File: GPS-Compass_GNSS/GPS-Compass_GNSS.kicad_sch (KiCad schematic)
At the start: 35 parts, among them J1 SMA_F, J3 01x10, Q1 MMBT3904, SW1 GNSS_RST, U1 BGA725L6E6327FTSA1, U2 TESEO-LIV3R

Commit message: asdas
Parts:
- J1: Antenna (none) -> https://cz.mouser.com/ProductDetail/Quectel/YEGT001AA?qs=7D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

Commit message: updates on different boards
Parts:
- added J4: 636101112001, gps-compass_brd:636101112001, symbol gps-compass_sch:636101112001
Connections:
- net GND: now also J4.1, J4.2
- net GNSS_ANT: now also J4.3
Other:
- moved on the sheet: C1, C2, C3, FL1, J1, L1, U1

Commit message: 3d and PCB
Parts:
- removed J1: SMA_F, Connector_Coaxial:SMA_BAT_Wireless_BWSMA-KWE-Z001, symbol Connector:Conn_Coaxial_Small

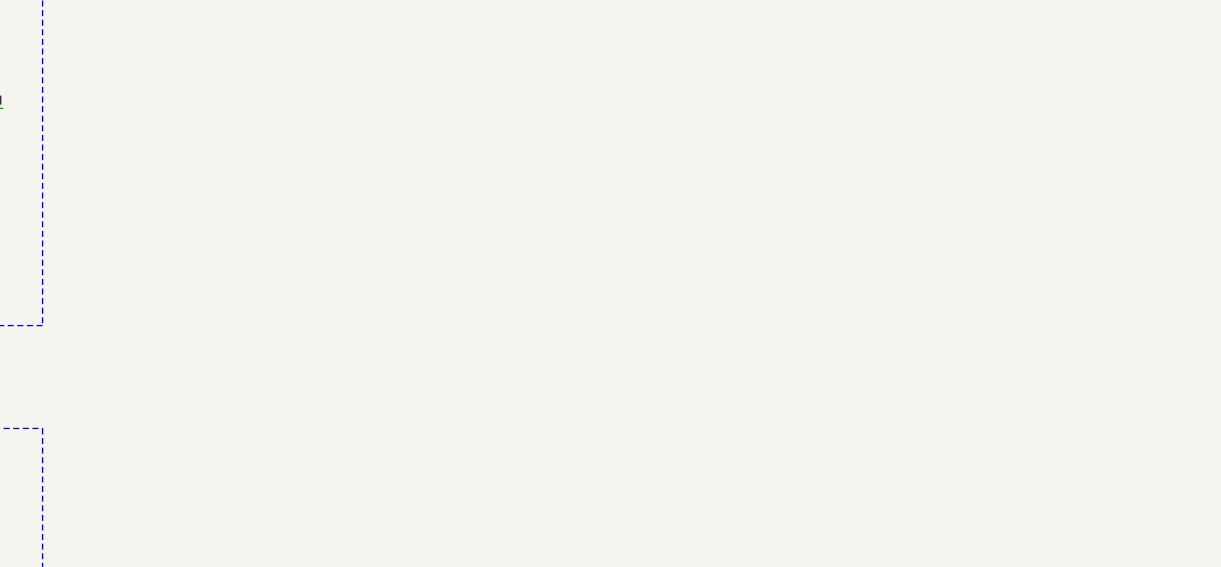
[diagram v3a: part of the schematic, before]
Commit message: new renders and 3d updat4ws
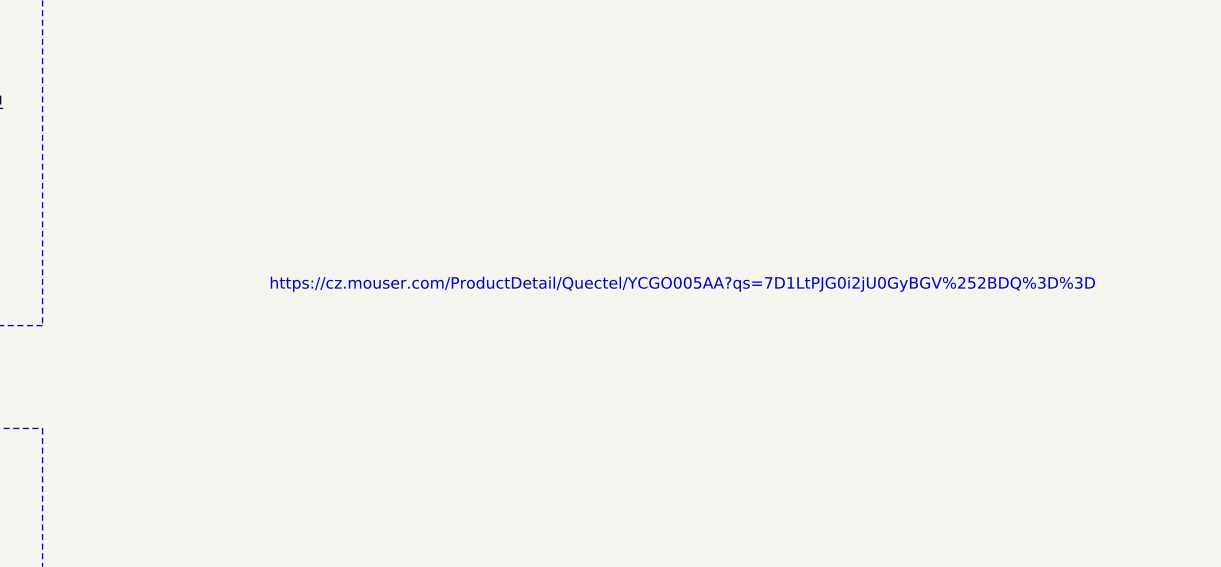
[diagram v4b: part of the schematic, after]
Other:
- note added: "https://cz.mouser.com/ProductDetail/Quectel/YCGO005AA?qs=7D1LtPJG0i2jU0GyBGV%252BDQ%3D%3D"

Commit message: BOM update
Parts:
- added AE1: Antenna, symbol Device:Antenna
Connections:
- no-connect marks 2 -> 3
